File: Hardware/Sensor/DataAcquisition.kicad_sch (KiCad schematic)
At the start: 34 parts, among them J1 Conn_01x16_Female, J2 Conn_01x16_Female, J7 UART, J8 USB_B_Micro, J9 Conn_01x04, Q6 Q_PMOS_GDS, Q7 Q_NMOS_GDS, U5 STM8S105K4B6, Y1 Crystal

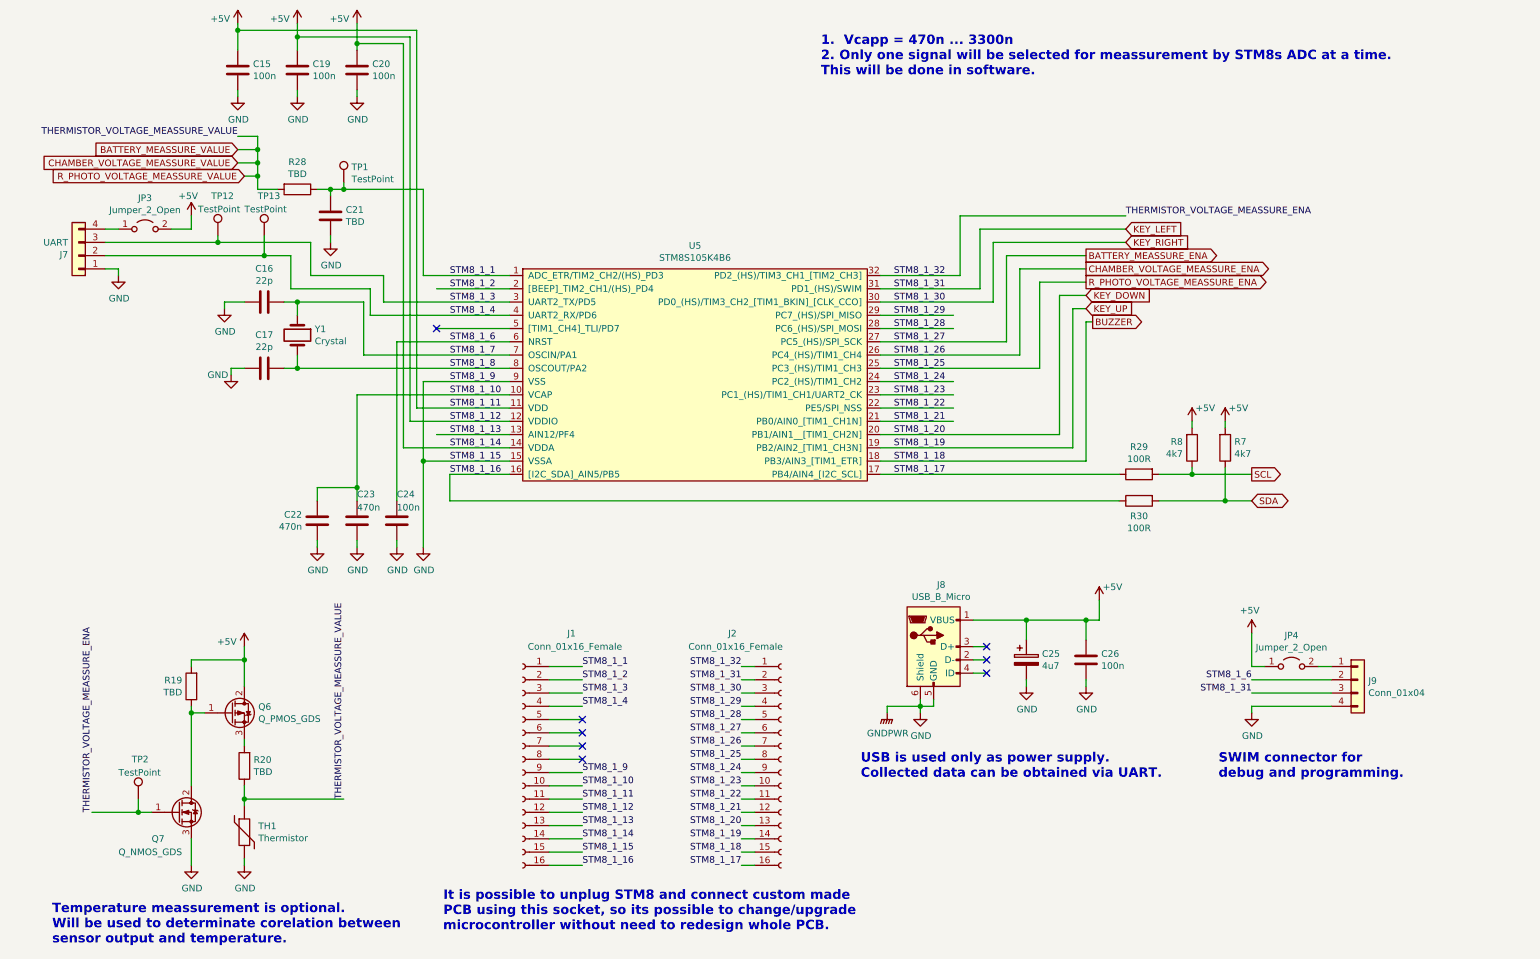
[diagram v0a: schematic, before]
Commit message: this is what was send for pcb production
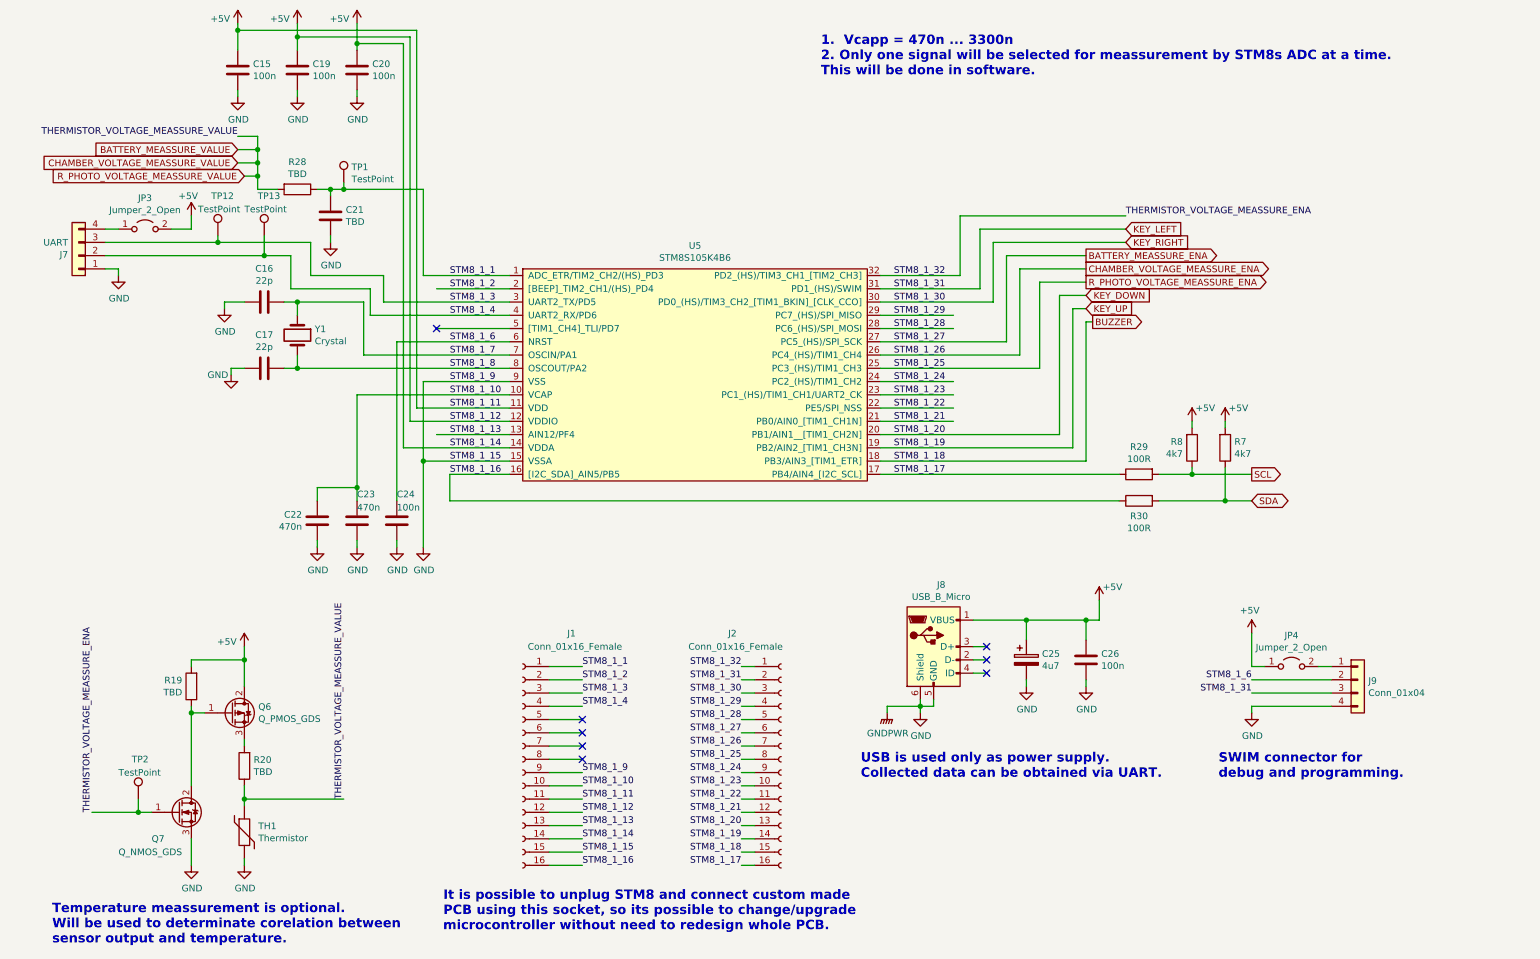
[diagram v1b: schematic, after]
